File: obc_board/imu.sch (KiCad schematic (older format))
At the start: 6 parts

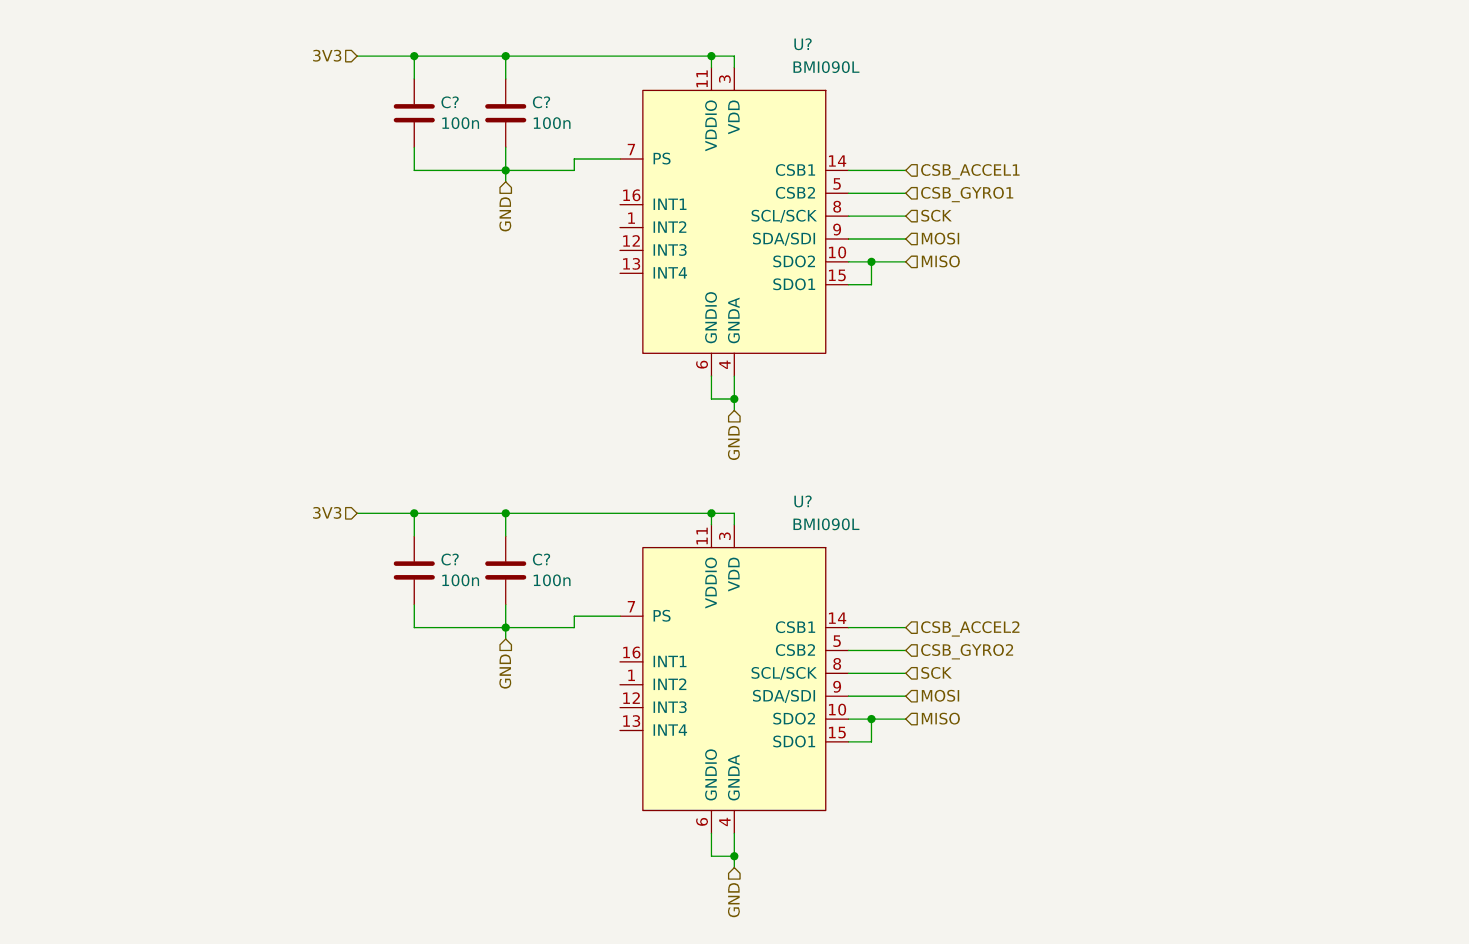
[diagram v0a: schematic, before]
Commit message: add imu and mux
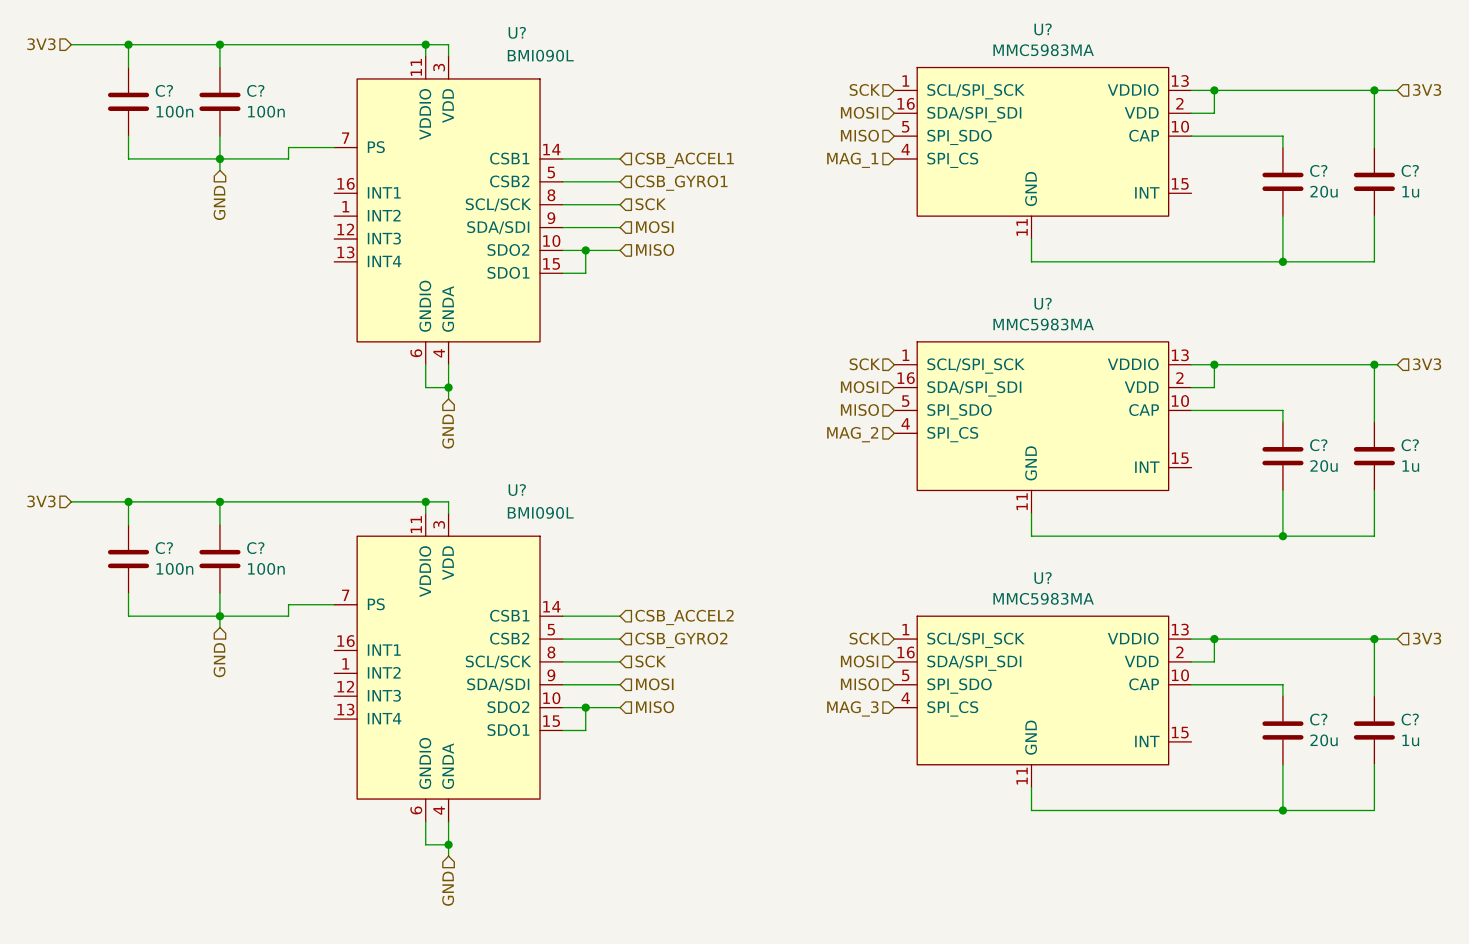
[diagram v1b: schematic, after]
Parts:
- added C? (x3): 20u, symbol Device:C
- added C? (x3): 1u, symbol Device:C
- added U? (x3): MMC5983MA, symbol cubesat_obc_lib:MMC5983MA
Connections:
- net 3V3: now also C?.1, C?.1, C?.1, U?.13 (VDDIO), U?.13 (VDDIO), U?.13 (VDDIO), U?.2 (VDD), U?.2 (VDD), U?.2 (VDD)
- net GND: now also C?.2, C?.2, C?.2, C?.2, C?.2, C?.2, U?.11 (GND), U?.11 (GND), U?.11 (GND), U?.9 (GND), U?.9 (GND), U?.9 (GND)
- net MISO: now also U?.5 (SPI_SDO), U?.5 (SPI_SDO), U?.5 (SPI_SDO)
- net MOSI: now also U?.16 (SDA/SPI_SDI), U?.16 (SDA/SPI_SDI), U?.16 (SDA/SPI_SDI)
- net SCK: now also U?.1 (SCL/SPI_SCK), U?.1 (SCL/SPI_SCK), U?.1 (SCL/SPI_SCK)
- new net: C?.1, U?.10 (CAP) (x3)
- new net: U?.12 (NC), U?.14 (NC), U?.3 (NC), U?.6 (NC), U?.7 (NC), U?.8 (NC) (x3)
- new net MAG_1: U?.4 (SPI_CS)
- new net MAG_2: U?.4 (SPI_CS)
- new net MAG_3: U?.4 (SPI_CS)
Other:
- moved on the sheet: C?, U?

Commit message: added h bridge and magnetometers
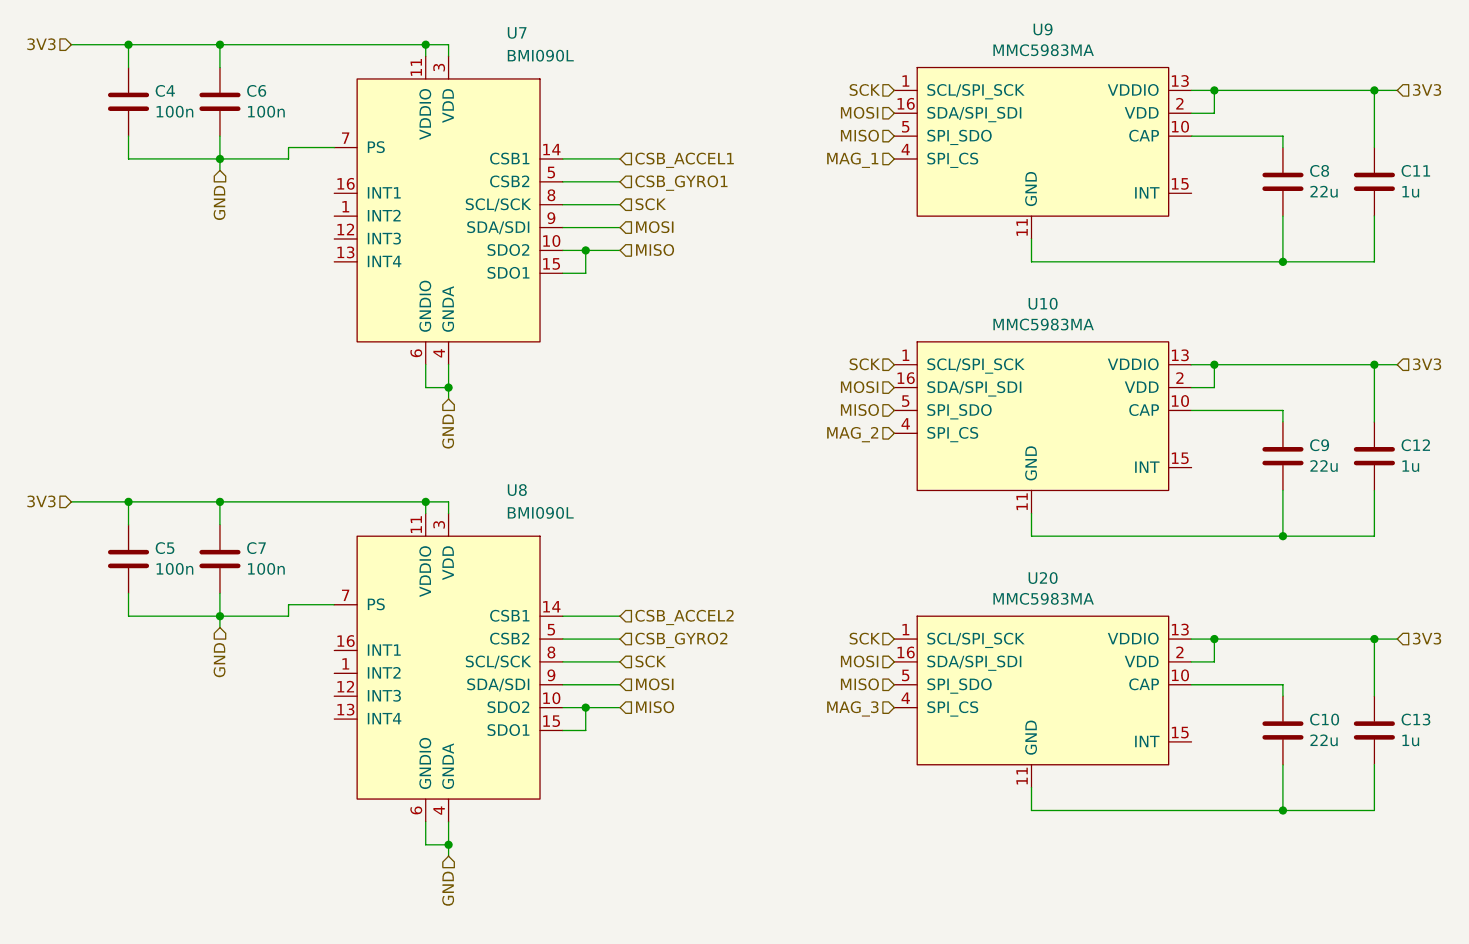
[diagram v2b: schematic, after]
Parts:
- C10, C8, C9: renamed from C?; value 20u -> 22u; footprint (none) -> Capacitor_SMD:C_1206_3216Metric; Digikey Part Number (none) -> 311-1995-1-ND
- C11, C12, C13: renamed from C?; footprint (none) -> Capacitor_SMD:C_0603_1608Metric; Digikey Part Number (none) -> 311-1446-2-ND
- U10, U20, U9: renamed from U?; footprint (none) -> Package_LGA:LGA-16_3x3mm_P0.5mm; Digikey Part Number (none) -> 1267-MMC5983MACT-ND
- U7, U8: renamed from U?; Digikey Part Number (none) -> 828-BMI090LCT-ND
- gave numbers to parts that had none: 4
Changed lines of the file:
@@
 $Descr A4 11693 8268
 encoding utf-8
-Sheet 9 9
+Sheet 8 10
 Title ""
 Date ""
@@
 $EndDescr
 $Comp
-L cubesat_obc_lib:BMI090L U?
+L cubesat_obc_lib:BMI090L U7
 U 1 1 5F9F0780
 P 4600 2700
-F 0 "U?" H 4900 3300 50  0000 C CNN
+F 0 "U7" H 4900 3300 50  0000 C CNN
 F 1 "BMI090L" H 5000 3200 50  0000 C CNN
 F 2 "cubesat_obc:PQFN50P450X300X100-16N" H 4600 2700 50  0001 C CNN
 F 3 "https://media.digikey.com/pdf/Data%20Sheets/Bosch/BST-BMI090L-DS000-00.pdf" H 4600 2700 50  0001 C CNN
+F 4 "828-BMI090LCT-ND" H 4600 2700 50  0001 C CNN "Digikey Part Number"
 	1    4600 2700
 	1    0    0    -1
@@
 	3600 2250 3600 2150
 $Comp
-L Device:C C?
+L Device:C C6
 U 1 1 5F9F07A0
 P 3600 2400
-F 0 "C?" H 3715 2446 50  0000 L CNN
+F 0 "C6" H 3715 2446 50  0000 L CNN
 F 1 "100n" H 3715 2355 50  0000 L CNN
 F 2 "Capacitor_SMD:C_0402_1005Metric" H 3638 2250 50  0001 C CNN
@@
 	2950 2150 3200 2150
 $Comp
-L Device:C C?
+L Device:C C4
 U 1 1 5F9F07A8
 P 3200 2400
-F 0 "C?" H 3315 2446 50  0000 L CNN
+F 0 "C4" H 3315 2446 50  0000 L CNN
 F 1 "100n" H 3315 2355 50  0000 L CNN
 F 2 "Capacitor_SMD:C_0402_1005Metric" H 3238 2250 50  0001 C CNN
@@
 	3900 2650 3600 2650
 $Comp
-L cubesat_obc_lib:BMI090L U?
+L cubesat_obc_lib:BMI090L U8
 U 1 1 5F9F07BD
 P 4600 4700
-F 0 "U?" H 4900 5300 50  0000 C CNN
+F 0 "U8" H 4900 5300 50  0000 C CNN
 F 1 "BMI090L" H 5000 5200 50  0000 C CNN
 F 2 "cubesat_obc:PQFN50P450X300X100-16N" H 4600 4700 50  0001 C CNN
 F 3 "https://media.digikey.com/pdf/Data%20Sheets/Bosch/BST-BMI090L-DS000-00.pdf" H 4600 4700 50  0001 C CNN
+F 4 "828-BMI090LCT-ND" H 4600 4700 50  0001 C CNN "Digikey Part Number"
 	1    4600 4700
 	1    0    0    -1
@@
 	3600 4250 3600 4150
 $Comp
-L Device:C C?
+L Device:C C7
 U 1 1 5F9F07DD
 P 3600 4400
-F 0 "C?" H 3715 4446 50  0000 L CNN
+F 0 "C7" H 3715 4446 50  0000 L CNN
 F 1 "100n" H 3715 4355 50  0000 L CNN
 F 2 "Capacitor_SMD:C_0402_1005Metric" H 3638 4250 50  0001 C CNN
@@
 	2950 4150 3200 4150
 $Comp
-L Device:C C?
+L Device:C C5
 U 1 1 5F9F07E5
 P 3200 4400
-F 0 "C?" H 3315 4446 50  0000 L CNN
+F 0 "C5" H 3315 4446 50  0000 L CNN
 F 1 "100n" H 3315 4355 50  0000 L CNN
 F 2 "Capacitor_SMD:C_0402_1005Metric" H 3238 4250 50  0001 C CNN
@@
 	3900 4650 3600 4650
 $Comp
-L cubesat_obc_lib:MMC5983MA U?
+L cubesat_obc_lib:MMC5983MA U9
 U 1 1 5FF9B4D5
 P 7200 2500
-F 0 "U?" H 7200 2915 50  0000 C CNN
+F 0 "U9" H 7200 2915 50  0000 C CNN
 F 1 "MMC5983MA" H 7200 2824 50  0000 C CNN
-F 2 "" H 7200 2500 50  0001 C CNN
-F 3 "" H 7200 2500 50  0001 C CNN
+F 2 "Package_LGA:LGA-16_3x3mm_P0.5mm" H 7200 2500 50  0001 C CNN
+F 3 "https://media.digikey.com/pdf/Data%20Sheets/MEMSIC%20PDFs/MMC5983MA_RevA_4-3-19.pdf" H 7200 2500 50  0001 C CNN
+F 4 "1267-MMC5983MACT-ND" H 7200 2500 50  0001 C CNN "Digikey Part Number"
 	1    7200 2500
 	1    0    0    -1
@@
 3V3
 $Comp
-L Device:C C?
+L Device:C C8
 U 1 1 5FFA46B0
 P 8250 2750
-F 0 "C?" H 8365 2796 50  0000 L CNN
-F 1 "20u" H 8365 2705 50  0000 L CNN
-F 2 "" H 8288 2600 50  0001 C CNN
-F 3 "~" H 8250 2750 50  0001 C CNN
+F 0 "C8" H 8365 2796 50  0000 L CNN
+F 1 "22u" H 8365 2705 50  0000 L CNN
+F 2 "Capacitor_SMD:C_1206_3216Metric" H 8288 2600 50  0001 C CNN
+F 3 "https://www.yageo.com/upload/media/product/productsearch/datasheet/mlcc/UPY-GPHC_X5R_4V-to-50V_26.pdf" H 8250 2750 50  0001 C CNN
+F 4 "311-1995-1-ND" H 8250 2750 50  0001 C CNN "Digikey Part Number"
 	1    8250 2750
 	1    0    0    -1
 $EndComp
 $Comp
-L Device:C C?
+L Device:C C11
 U 1 1 5FFA600C
 P 8650 2750
-F 0 "C?" H 8765 2796 50  0000 L CNN
+F 0 "C11" H 8765 2796 50  0000 L CNN
 F 1 "1u" H 8765 2705 50  0000 L CNN
-F 2 "" H 8688 2600 50  0001 C CNN
-F 3 "~" H 8650 2750 50  0001 C CNN
+F 2 "Capacitor_SMD:C_0603_1608Metric" H 8688 2600 50  0001 C CNN
+F 3 "https://www.yageo.com/upload/media/product/productsearch/datasheet/mlcc/UPY-GPHC_X7R_6.3V-to-50V_18.pdf" H 8650 2750 50  0001 C CNN
+F 4 "311-1446-2-ND" H 8650 2750 50  0001 C CNN "Digikey Part Number"
 	1    8650 2750
 	1    0    0    -1
@@
 	8650 2350 7950 2350
 $Comp
-L cubesat_obc_lib:MMC5983MA U?
+L cubesat_obc_lib:MMC5983MA U10
 U 1 1 5FFB52A6
 P 7200 3700
-F 0 "U?" H 7200 4115 50  0000 C CNN
+F 0 "U10" H 7200 4115 50  0000 C CNN
 F 1 "MMC5983MA" H 7200 4024 50  0000 C CNN
-F 2 "" H 7200 3700 50  0001 C CNN
-F 3 "" H 7200 3700 50  0001 C CNN
+F 2 "Package_LGA:LGA-16_3x3mm_P0.5mm" H 7200 3700 50  0001 C CNN
+F 3 "https://media.digikey.com/pdf/Data%20Sheets/MEMSIC%20PDFs/MMC5983MA_RevA_4-3-19.pdf" H 7200 3700 50  0001 C CNN
+F 4 "1267-MMC5983MACT-ND" H 7200 3700 50  0001 C CNN "Digikey Part Number"
 	1    7200 3700
 	1    0    0    -1
@@
 3V3
 $Comp
-L Device:C C?
+L Device:C C9
 U 1 1 5FFB52B0
 P 8250 3950
-F 0 "C?" H 8365 3996 50  0000 L CNN
-F 1 "20u" H 8365 3905 50  0000 L CNN
-F 2 "" H 8288 3800 50  0001 C CNN
-F 3 "~" H 8250 3950 50  0001 C CNN
+F 0 "C9" H 8365 3996 50  0000 L CNN
+F 1 "22u" H 8365 3905 50  0000 L CNN
+F 2 "Capacitor_SMD:C_1206_3216Metric" H 8288 3800 50  0001 C CNN
+F 3 "https://www.yageo.com/upload/media/product/productsearch/datasheet/mlcc/UPY-GPHC_X5R_4V-to-50V_26.pdf" H 8250 3950 50  0001 C CNN
+F 4 "311-1995-1-ND" H 8250 3950 50  0001 C CNN "Digikey Part Number"
 	1    8250 3950
 	1    0    0    -1
 $EndComp
 $Comp
-L Device:C C?
+L Device:C C12
 U 1 1 5FFB52B6
 P 8650 3950
-F 0 "C?" H 8765 3996 50  0000 L CNN
+F 0 "C12" H 8765 3996 50  0000 L CNN
 F 1 "1u" H 8765 3905 50  0000 L CNN
-F 2 "" H 8688 3800 50  0001 C CNN
-F 3 "~" H 8650 3950 50  0001 C CNN
+F 2 "Capacitor_SMD:C_0603_1608Metric" H 8688 3800 50  0001 C CNN
+F 3 "https://www.yageo.com/upload/media/product/productsearch/datasheet/mlcc/UPY-GPHC_X7R_6.3V-to-50V_18.pdf" H 8650 3950 50  0001 C CNN
+F 4 "311-1446-2-ND" H 8650 3950 50  0001 C CNN "Digikey Part Number"
 	1    8650 3950
 	1    0    0    -1
@@
 	8650 3550 7950 3550
 $Comp
-L cubesat_obc_lib:MMC5983MA U?
+L cubesat_obc_lib:MMC5983MA U20
 U 1 1 5FFB7DFF
 P 7200 4900
-F 0 "U?" H 7200 5315 50  0000 C CNN
+F 0 "U20" H 7200 5315 50  0000 C CNN
 F 1 "MMC5983MA" H 7200 5224 50  0000 C CNN
-F 2 "" H 7200 4900 50  0001 C CNN
-F 3 "" H 7200 4900 50  0001 C CNN
+F 2 "Package_LGA:LGA-16_3x3mm_P0.5mm" H 7200 4900 50  0001 C CNN
+F 3 "https://media.digikey.com/pdf/Data%20Sheets/MEMSIC%20PDFs/MMC5983MA_RevA_4-3-19.pdf" H 7200 4900 50  0001 C CNN
+F 4 "1267-MMC5983MACT-ND" H 7200 4900 50  0001 C CNN "Digikey Part Number"
 	1    7200 4900
 	1    0    0    -1
@@
 3V3
 $Comp
-L Device:C C?
+L Device:C C10
 U 1 1 5FFB7E09
 P 8250 5150
-F 0 "C?" H 8365 5196 50  0000 L CNN
-F 1 "20u" H 8365 5105 50  0000 L CNN
-F 2 "" H 8288 5000 50  0001 C CNN
-F 3 "~" H 8250 5150 50  0001 C CNN
+F 0 "C10" H 8365 5196 50  0000 L CNN
+F 1 "22u" H 8365 5105 50  0000 L CNN
+F 2 "Capacitor_SMD:C_1206_3216Metric" H 8288 5000 50  0001 C CNN
+F 3 "https://www.yageo.com/upload/media/product/productsearch/datasheet/mlcc/UPY-GPHC_X5R_4V-to-50V_26.pdf" H 8250 5150 50  0001 C CNN
+F 4 "311-1995-1-ND" H 8250 5150 50  0001 C CNN "Digikey Part Number"
 	1    8250 5150
 	1    0    0    -1
 $EndComp
 $Comp
-L Device:C C?
+L Device:C C13
 U 1 1 5FFB7E0F
 P 8650 5150
-F 0 "C?" H 8765 5196 50  0000 L CNN
+F 0 "C13" H 8765 5196 50  0000 L CNN
 F 1 "1u" H 8765 5105 50  0000 L CNN
-F 2 "" H 8688 5000 50  0001 C CNN
-F 3 "~" H 8650 5150 50  0001 C CNN
+F 2 "Capacitor_SMD:C_0603_1608Metric" H 8688 5000 50  0001 C CNN
+F 3 "https://www.yageo.com/upload/media/product/productsearch/datasheet/mlcc/UPY-GPHC_X7R_6.3V-to-50V_18.pdf" H 8650 5150 50  0001 C CNN
+F 4 "311-1446-2-ND" H 8650 5150 50  0001 C CNN "Digikey Part Number"
 	1    8650 5150
 	1    0    0    -1
